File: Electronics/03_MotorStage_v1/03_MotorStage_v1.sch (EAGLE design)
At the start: 73 parts, among them J1 BARRIER_BLOCK-2PIN, J2 BARRIER_BLOCK-5PIN, J3 CONN_2X3_SMD, U1 XL4016-DEV

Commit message: Motor stage circuit board v1 final
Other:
- note added: "Brass Standoffs"
- note added: "Header Interface to Power Management Board"
- note added: "Hippo-PS Motor Stage Designed by: Erin Kennedy July 9, 2022"
- note added: "Linear Regulators for Motor Drivers"
- note added: "Output of Linear Regulators"
- note added: "Output of Switching Regulator"
- note added: "Switching Regulator Module"
- note added: "Testpoints (Switching V+, Battery In+)"
- note added: "Voltage Divider and LED (for switching regulator)"
- moved on the sheet: C10, C3, C4, C5, C6, C7, C8, C9, D1, D2, D3, D4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

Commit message: Naming update to Hippo-PD
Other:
- note added: "Hippo-PD Motor Stage Designed by: Erin Kennedy July 9, 2022"
- note removed: "Hippo-PS Motor Stage Designed by: Erin Kennedy July 9, 2022"
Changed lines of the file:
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@@
 <text x="10.16" y="66.04" size="2.54" layer="95">Testpoints (Switching V+, Battery In+)</text>
 <text x="15.24" y="111.76" size="2.54" layer="95">Output of Switching Regulator</text>
-<text x="149.86" y="25.4" size="1.778" layer="95">Hippo-PS Motor Stage
+<text x="149.86" y="25.4" size="1.778" layer="95">Hippo-PD Motor Stage
 Designed by: Erin Kennedy
 July 9, 2022</text>
@@
 <plain>
 <text x="91.44" y="175.26" size="2.54" layer="95">Linear Regulators for Motor Drivers</text>
-<text x="149.86" y="25.4" size="1.778" layer="95">Hippo-PS Motor Stage
+<text x="149.86" y="25.4" size="1.778" layer="95">Hippo-PD Motor Stage
 Designed by: Erin Kennedy
 July 9, 2022</text>

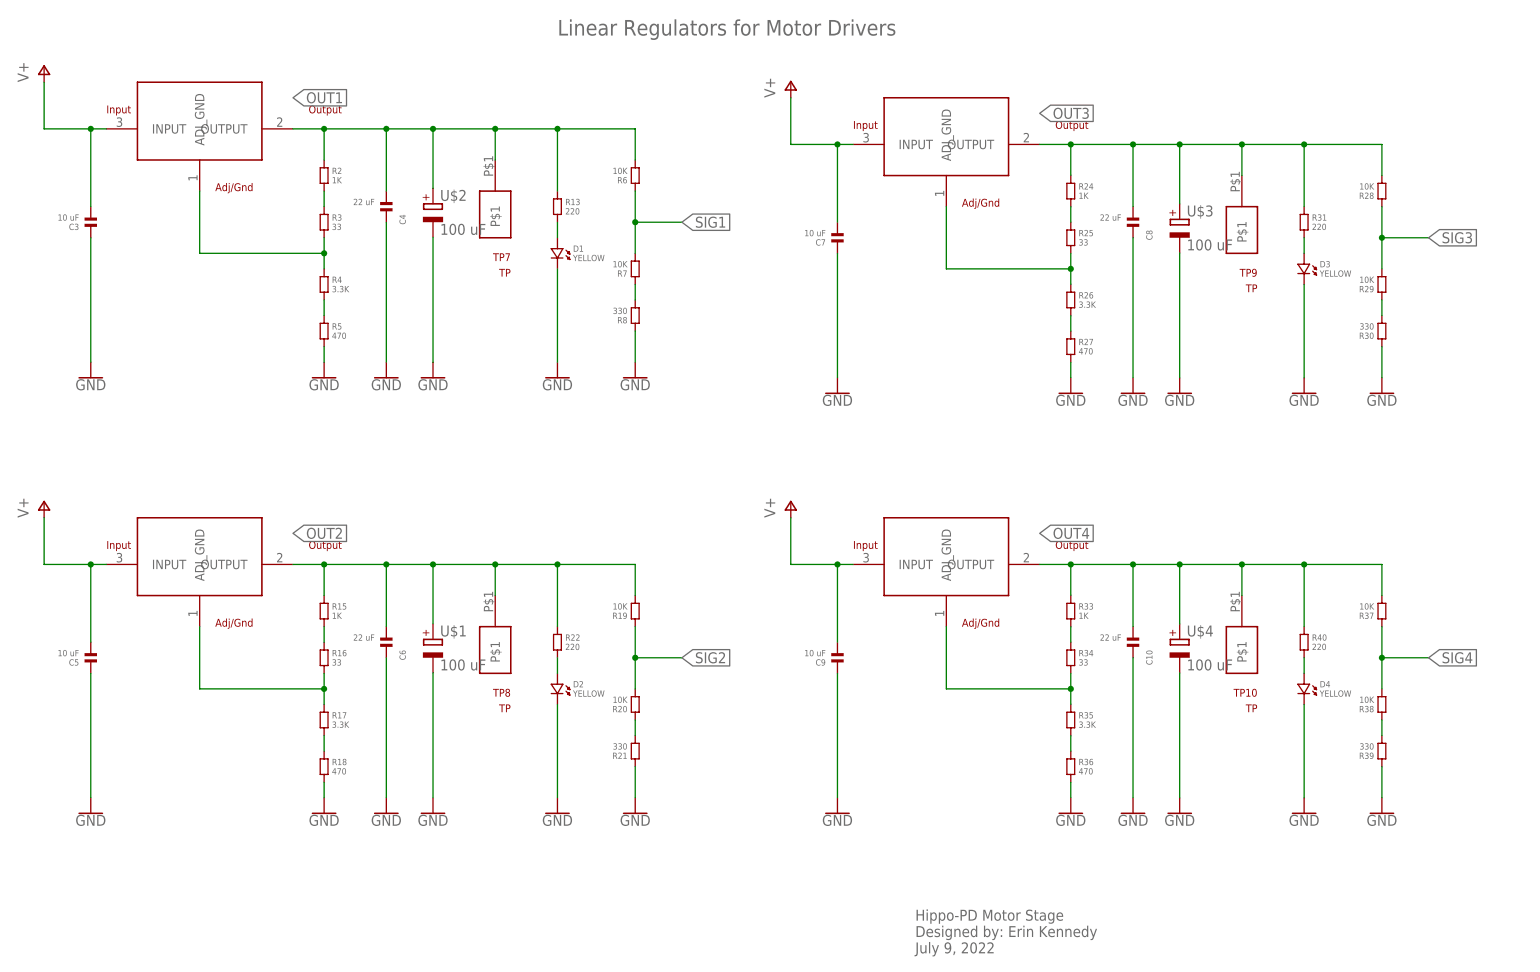
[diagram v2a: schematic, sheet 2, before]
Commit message: Updated refdes of some components
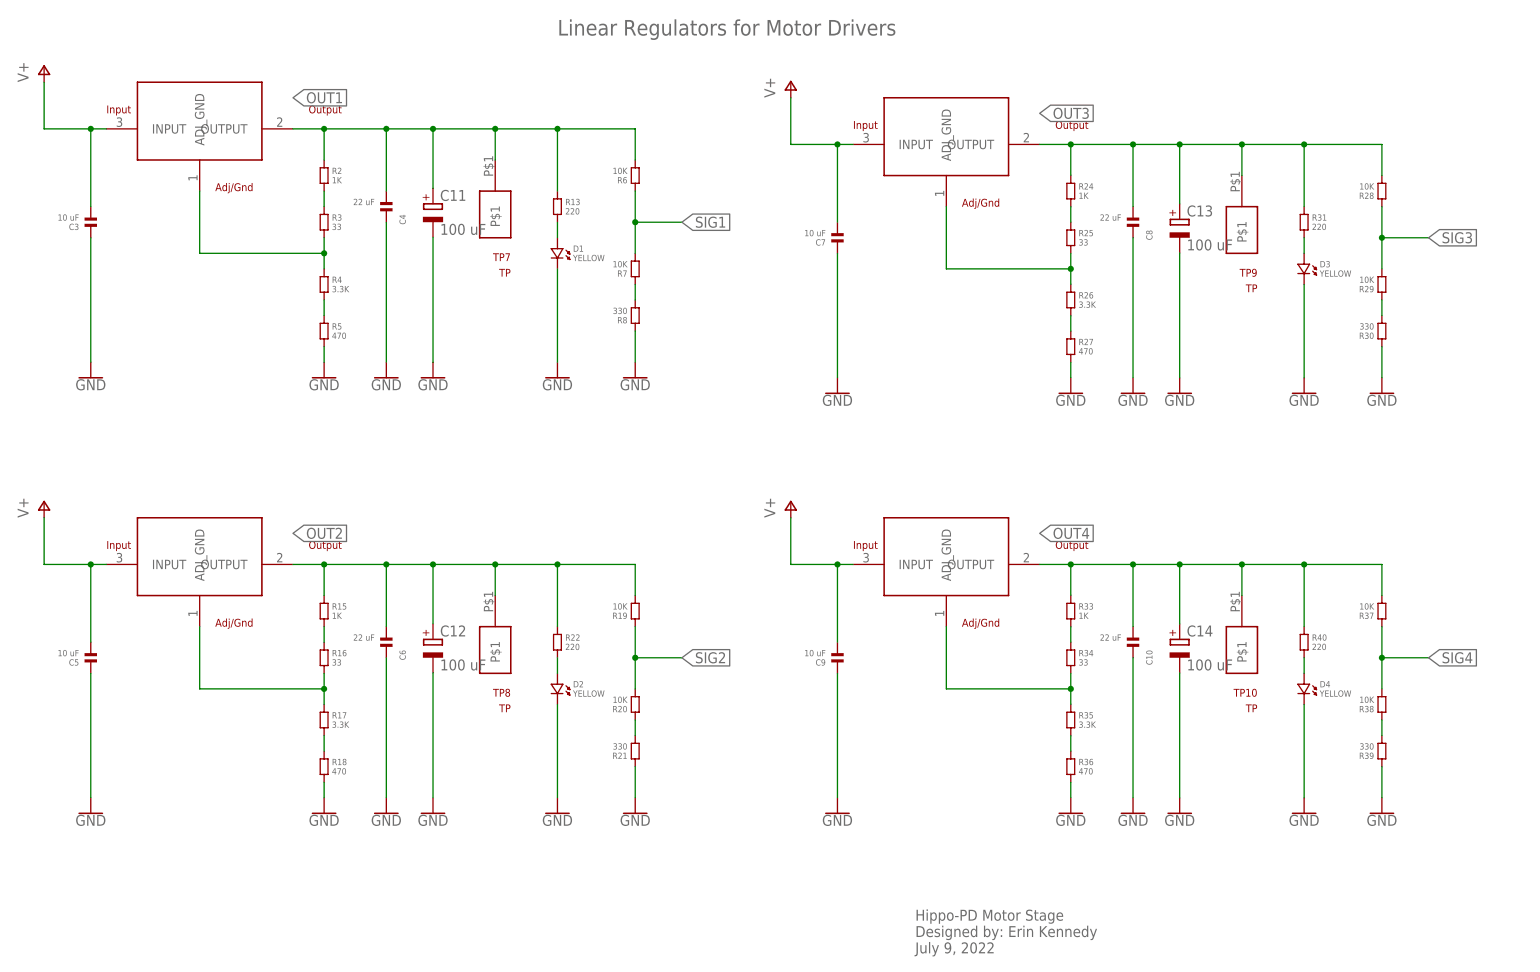
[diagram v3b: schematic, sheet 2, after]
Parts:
- renumbered R1 to U2, R14 to U3, R23 to U4, R32 to U5, U$1 to C12, U$2 to C11, U$3 to C13, U$4 to C14
